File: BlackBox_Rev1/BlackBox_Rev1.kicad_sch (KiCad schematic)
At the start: 17 parts, among them J1 RJ45_LED_Shielded, J2 Molex_uF_SV_06, J3 Conn_02x08_Counter_Clockwise, SW1 SW_Push, SW2 SW_Push, U1 Teensy4.1_DEV-16771, U2 TSR1-2433

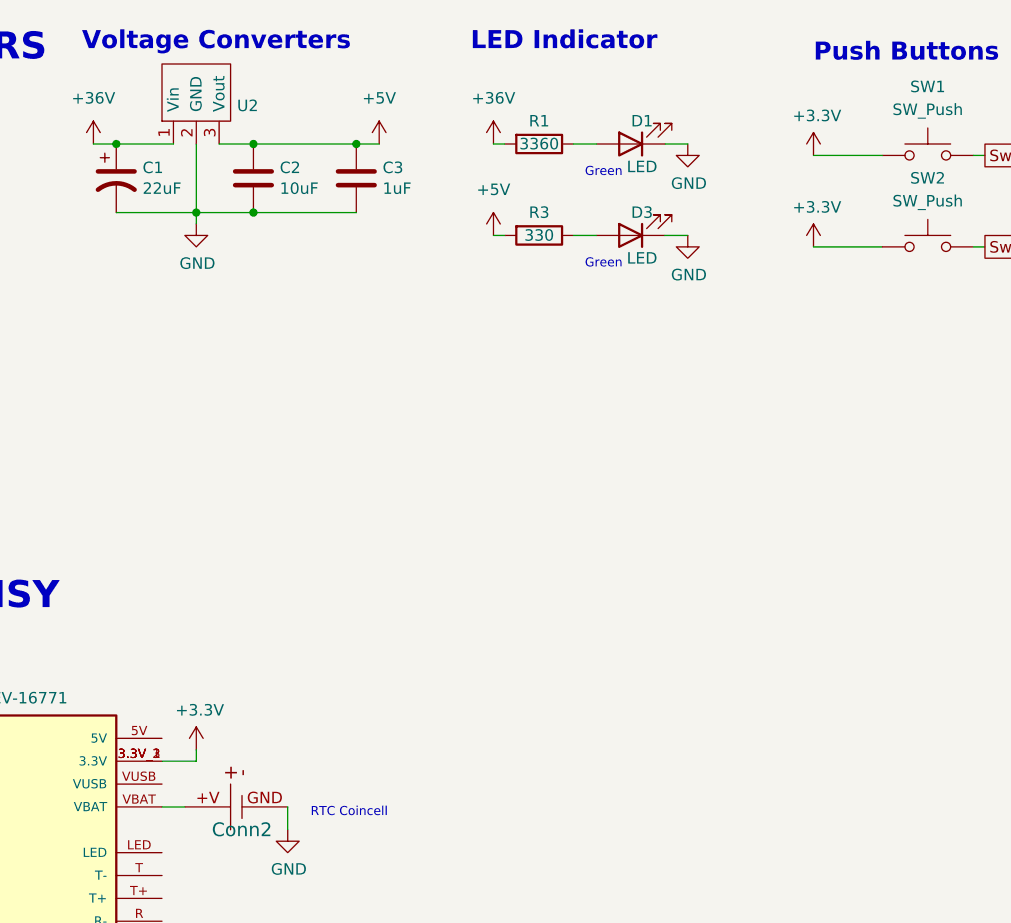
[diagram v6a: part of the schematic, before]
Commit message: switch 3v3 oki to 5v
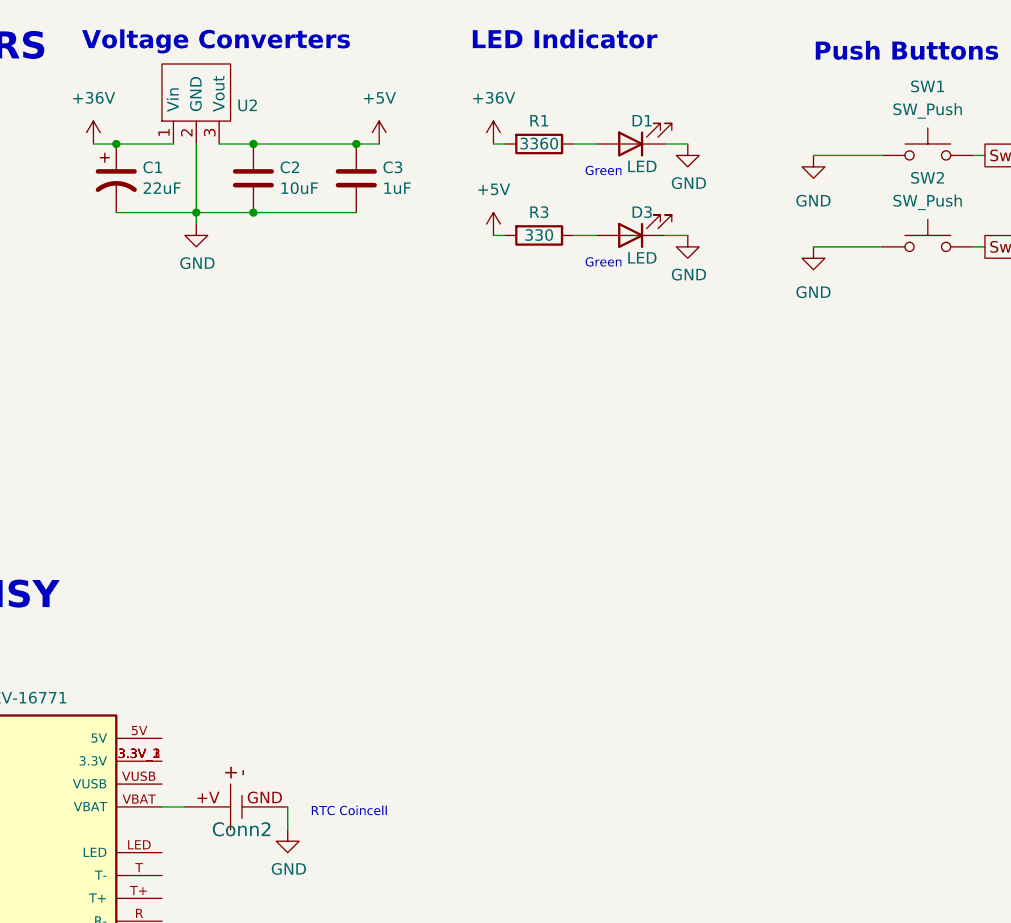
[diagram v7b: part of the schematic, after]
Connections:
- net GND: now also SW1.1, SW2.1
- net +3V3: no longer names the net of U1.3.3V_1 (3.3V), U1.3.3V_2 (3.3V), U1.3.3V_3 (3.3V)
- net +3V3: no longer SW1.1, SW2.1
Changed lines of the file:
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@@
-    (stroke (width 0) (type default) (color 0 0 0 0))
-  )
-  (wire (pts (xy 63.5 95.25) (xy 67.31 95.25))
     (stroke (width 0) (type default) (color 0 0 0 0))
   )
@@
   )
   (wire (pts (xy 111.76 177.8) (xy 104.14 177.8))
-    (stroke (width 0) (type default) (color 0 0 0 0))
-  )
-  (wire (pts (xy 67.31 95.25) (xy 67.31 93.98))
     (stroke (width 0) (type default) (color 0 0 0 0))
   )
@@
     (pin "2")
   )
-  (symbol (lib_id "BMS_2022_Rev1-rescue:+3.3V-power") (at 135.89 27.94 0) (unit 1)
-    (in_bom yes) (on_board yes)
-    (property "Reference" "#PWR014" (id 0) (at 135.89 31.75 0)
-      (effects (font (size 1.27 1.27)) hide)
-    )
-    (property "Value" "+3.3V" (id 1) (at 136.271 23.5458 0))
+  (symbol (lib_id "power:GND") (at 135.89 27.94 0) (unit 1)
+    (in_bom yes) (on_board yes) (fields_autoplaced)
+    (property "Reference" "#PWR?" (id 0) (at 135.89 34.29 0)
+      (effects (font (size 1.27 1.27)) hide)
+    )
+    (property "Value" "GND" (id 1) (at 135.89 33.02 0))
     (property "Footprint" "" (id 2) (at 135.89 27.94 0)
       (effects (font (size 1.27 1.27)) hide)
@@
     (pin "GND")
   )
-  (symbol (lib_id "BMS_2022_Rev1-rescue:+3.3V-power") (at 135.89 38.1 0) (unit 1)
-    (in_bom yes) (on_board yes)
-    (property "Reference" "#PWR015" (id 0) (at 135.89 41.91 0)
-      (effects (font (size 1.27 1.27)) hide)
-    )
-    (property "Value" "+3.3V" (id 1) (at 136.271 33.7058 0))
-    (property "Footprint" "" (id 2) (at 135.89 38.1 0)
-      (effects (font (size 1.27 1.27)) hide)
-    )
-    (property "Datasheet" "" (id 3) (at 135.89 38.1 0)
-      (effects (font (size 1.27 1.27)) hide)
-    )
-    (pin "1")
-  )
-  (symbol (lib_id "BMS_2022_Rev1-rescue:+3.3V-power") (at 67.31 93.98 0) (unit 1)
-    (in_bom yes) (on_board yes)
-    (property "Reference" "#PWR05" (id 0) (at 67.31 97.79 0)
-      (effects (font (size 1.27 1.27)) hide)
-    )
-    (property "Value" "+3.3V" (id 1) (at 67.691 89.5858 0))
-    (property "Footprint" "" (id 2) (at 67.31 93.98 0)
-      (effects (font (size 1.27 1.27)) hide)
-    )
-    (property "Datasheet" "" (id 3) (at 67.31 93.98 0)
-      (effects (font (size 1.27 1.27)) hide)
-    )
-    (pin "1")
-  )
   (symbol (lib_id "power:+36V") (at 55.88 26.67 0) (unit 1)
     (in_bom yes) (on_board yes) (fields_autoplaced)
@@
     )
     (property "Datasheet" "" (id 3) (at 87.63 26.67 0)
+      (effects (font (size 1.27 1.27)) hide)
+    )
+    (pin "1")
+  )
+  (symbol (lib_id "power:GND") (at 135.89 38.1 0) (unit 1)
+    (in_bom yes) (on_board yes) (fields_autoplaced)
+    (property "Reference" "#PWR?" (id 0) (at 135.89 44.45 0)
+      (effects (font (size 1.27 1.27)) hide)
+    )
+    (property "Value" "GND" (id 1) (at 135.89 43.18 0))
+    (property "Footprint" "" (id 2) (at 135.89 38.1 0)
+      (effects (font (size 1.27 1.27)) hide)
+    )
+    (property "Datasheet" "" (id 3) (at 135.89 38.1 0)
       (effects (font (size 1.27 1.27)) hide)
     )
@@
       (reference "#PWR04") (unit 1) (value "GND") (footprint "")
     )
-    (path "/958bbc9f-66a0-4604-9b6d-d3621440c2de"
-      (reference "#PWR05") (unit 1) (value "+3.3V") (footprint "")
-    )
     (path "/722f77bd-ce71-49bf-bfda-194793b15f4c"
       (reference "#PWR06") (unit 1) (value "GND") (footprint "")
@@
       (reference "#PWR013") (unit 1) (value "GND") (footprint "")
     )
-    (path "/5b517e01-b023-4ad1-b431-775406243181"
-      (reference "#PWR014") (unit 1) (value "+3.3V") (footprint "")
-    )
-    (path "/93f53a53-69e3-4b19-9941-fb83ace603e9"
-      (reference "#PWR015") (unit 1) (value "+3.3V") (footprint "")
-    )
     (path "/ad13e068-7804-4b67-91fc-bdaf7841372b"
       (reference "#PWR0102") (unit 1) (value "+36V") (footprint "")
@@
       (reference "#PWR?") (unit 1) (value "+5V") (footprint "")
     )
+    (path "/491f5967-65fd-4965-bba8-1fe119080e6b"
+      (reference "#PWR?") (unit 1) (value "GND") (footprint "")
+    )
     (path "/6f88f0a5-e370-4733-af3c-1d17e91e8cb2"
       (reference "#PWR?") (unit 1) (value "+5V") (footprint "")
@@
       (reference "#PWR?") (unit 1) (value "+5V") (footprint "")
     )
+    (path "/b313c2d6-5ee0-44a2-adce-49b59090713f"
+      (reference "#PWR?") (unit 1) (value "GND") (footprint "")
+    )
     (path "/c66825b9-5143-4c83-90ee-8bd89d91f6cd"

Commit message: hotfix
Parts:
- Conn1: footprint MRDT_Connectors:Anderson_2_Horizontal_Side_by_Side -> MRDT_Connectors:Square_Anderson_2_H_Side_By_Side
- R1: value 3360 -> 2500
- R3: value 330 -> 200
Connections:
- net TX+: now reaches J1.1, J2.1
- net TX-: now reaches J1.3, J2.2
- net RX-: now reaches J1.6, J2.5
- net RX+: now reaches J1.4, J2.6
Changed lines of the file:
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@@
     (effects (font (size 3 3) (thickness 0.5994) bold) (justify left bottom))
+  )
+  (label "RX-" (at 106.68 166.37 0)
+    (effects (font (size 1.27 1.27)) (justify left bottom))
+  )
+  (label "RX+" (at 109.22 184.15 0)
+    (effects (font (size 1.27 1.27)) (justify left bottom))
+  )
+  (label "TX+" (at 93.98 180.34 0)
+    (effects (font (size 1.27 1.27)) (justify left bottom))
+  )
+  (label "TX-" (at 99.06 176.53 0)
+    (effects (font (size 1.27 1.27)) (justify left bottom))
   )
   (global_label "Display_G" (shape output) (at 22.86 151.13 180) (fields_autoplaced)
@@
       (effects (font (size 1.524 1.524)))
     )
-    (property "Footprint" "MRDT_Connectors:Anderson_2_Horizontal_Side_by_Side" (id 2) (at 25.4 39.37 0)
+    (property "Footprint" "MRDT_Connectors:Square_Anderson_2_H_Side_By_Side" (id 2) (at 25.4 39.37 0)
       (effects (font (size 1.524 1.524)) hide)
     )
@@
   (symbol (lib_id "power:+5V") (at 100.33 36.83 0) (unit 1)
     (in_bom yes) (on_board yes) (fields_autoplaced)
-    (property "Reference" "#PWR?" (id 0) (at 100.33 40.64 0)
+    (property "Reference" "#PWR0104" (id 0) (at 100.33 40.64 0)
       (effects (font (size 1.27 1.27)) hide)
     )
@@
       (effects (font (size 1.524 1.524)))
     )
-    (property "Footprint" "MRDT_Connectors:Anderson_2_Horizontal_Side_by_Side" (id 2) (at 25.4 45.72 0)
+    (property "Footprint" "MRDT_Connectors:Square_Anderson_2_H_Side_By_Side" (id 2) (at 25.4 45.72 0)
       (effects (font (size 1.524 1.524)) hide)
     )
@@
   (symbol (lib_id "power:GND") (at 135.89 27.94 0) (unit 1)
     (in_bom yes) (on_board yes) (fields_autoplaced)
-    (property "Reference" "#PWR?" (id 0) (at 135.89 34.29 0)
+    (property "Reference" "#PWR0106" (id 0) (at 135.89 34.29 0)
       (effects (font (size 1.27 1.27)) hide)
     )
@@
     (in_bom yes) (on_board yes)
     (property "Reference" "R3" (id 0) (at 105.41 34.29 90))
-    (property "Value" "330" (id 1) (at 105.41 36.83 90))
+    (property "Value" "200" (id 1) (at 105.41 36.83 90))
     (property "Footprint" "Resistor_SMD:R_0603_1608Metric_Pad0.98x0.95mm_HandSolder" (id 2) (at 105.41 35.052 90)
       (effects (font (size 1.27 1.27)) hide)
@@
   (symbol (lib_id "power:+5V") (at 21.59 105.41 0) (unit 1)
     (in_bom yes) (on_board yes) (fields_autoplaced)
-    (property "Reference" "#PWR?" (id 0) (at 21.59 109.22 0)
+    (property "Reference" "#PWR0101" (id 0) (at 21.59 109.22 0)
       (effects (font (size 1.27 1.27)) hide)
     )
@@
   (symbol (lib_id "power:+5V") (at 87.63 26.67 0) (unit 1)
     (in_bom yes) (on_board yes) (fields_autoplaced)
-    (property "Reference" "#PWR?" (id 0) (at 87.63 30.48 0)
+    (property "Reference" "#PWR0103" (id 0) (at 87.63 30.48 0)
       (effects (font (size 1.27 1.27)) hide)
     )
@@
   (symbol (lib_id "power:GND") (at 135.89 38.1 0) (unit 1)
     (in_bom yes) (on_board yes) (fields_autoplaced)
-    (property "Reference" "#PWR?" (id 0) (at 135.89 44.45 0)
+    (property "Reference" "#PWR0105" (id 0) (at 135.89 44.45 0)
       (effects (font (size 1.27 1.27)) hide)
     )
@@
     (in_bom yes) (on_board yes)
     (property "Reference" "R1" (id 0) (at 105.41 24.13 90))
-    (property "Value" "3360" (id 1) (at 105.41 26.67 90))
+    (property "Value" "2500" (id 1) (at 105.41 26.67 90))
     (property "Footprint" "Resistor_SMD:R_0603_1608Metric_Pad0.98x0.95mm_HandSolder" (id 2) (at 105.41 24.892 90)
       (effects (font (size 1.27 1.27)) hide)
@@
       (reference "#PWR013") (unit 1) (value "GND") (footprint "")
     )
+    (path "/6f88f0a5-e370-4733-af3c-1d17e91e8cb2"
+      (reference "#PWR0101") (unit 1) (value "+5V") (footprint "")
+    )
     (path "/ad13e068-7804-4b67-91fc-bdaf7841372b"
       (reference "#PWR0102") (unit 1) (value "+36V") (footprint "")
     )
+    (path "/b232c6a7-d1d3-411d-9ca8-7ee5db602648"
+      (reference "#PWR0103") (unit 1) (value "+5V") (footprint "")
+    )
     (path "/1dfb3293-a7d9-4442-b7df-5cdfc068440f"
-      (reference "#PWR?") (unit 1) (value "+5V") (footprint "")
+      (reference "#PWR0104") (unit 1) (value "+5V") (footprint "")
+    )
+    (path "/b313c2d6-5ee0-44a2-adce-49b59090713f"
+      (reference "#PWR0105") (unit 1) (value "GND") (footprint "")
     )
     (path "/491f5967-65fd-4965-bba8-1fe119080e6b"
-      (reference "#PWR?") (unit 1) (value "GND") (footprint "")
-    )
-    (path "/6f88f0a5-e370-4733-af3c-1d17e91e8cb2"
-      (reference "#PWR?") (unit 1) (value "+5V") (footprint "")
-    )
-    (path "/b232c6a7-d1d3-411d-9ca8-7ee5db602648"
-      (reference "#PWR?") (unit 1) (value "+5V") (footprint "")
-    )
-    (path "/b313c2d6-5ee0-44a2-adce-49b59090713f"
-      (reference "#PWR?") (unit 1) (value "GND") (footprint "")
+      (reference "#PWR0106") (unit 1) (value "GND") (footprint "")
     )
     (path "/c66825b9-5143-4c83-90ee-8bd89d91f6cd"
@@
     )
     (path "/2f60ec2a-4d0e-4380-b697-1527d0f87c85"
-      (reference "Conn1") (unit 1) (value "AndersonPP") (footprint "MRDT_Connectors:Anderson_2_Horizontal_Side_by_Side")
+      (reference "Conn1") (unit 1) (value "AndersonPP") (footprint "MRDT_Connectors:Square_Anderson_2_H_Side_By_Side")
     )
     (path "/0b89041a-45c9-40c3-804f-53fb5d5f1f43"
-      (reference "Conn1") (unit 2) (value "AndersonPP") (footprint "MRDT_Connectors:Anderson_2_Horizontal_Side_by_Side")
+      (reference "Conn1") (unit 2) (value "AndersonPP") (footprint "MRDT_Connectors:Square_Anderson_2_H_Side_By_Side")
     )
     (path "/747c4b61-0c76-42fb-ad21-bc0ce87b9d4a"
@@
     )
     (path "/ddcf5a1f-cc0e-4fde-9881-bf4cb26ea7d8"
-      (reference "R1") (unit 1) (value "3360") (footprint "Resistor_SMD:R_0603_1608Metric_Pad0.98x0.95mm_HandSolder")
+      (reference "R1") (unit 1) (value "2500") (footprint "Resistor_SMD:R_0603_1608Metric_Pad0.98x0.95mm_HandSolder")
     )
     (path "/6c3a7b5d-14f5-4b7a-b088-57780c520973"
-      (reference "R3") (unit 1) (value "330") (footprint "Resistor_SMD:R_0603_1608Metric_Pad0.98x0.95mm_HandSolder")
+      (reference "R3") (unit 1) (value "200") (footprint "Resistor_SMD:R_0603_1608Metric_Pad0.98x0.95mm_HandSolder")
     )
     (path "/42cc665b-a380-4c51-8f90-bb426bcc7d9f"
